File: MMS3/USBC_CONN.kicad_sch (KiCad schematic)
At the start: 7 parts, among them J800 USB_C_Receptacle_USB2.0_16P, U401 TPD2EUSB30DRTR-TP

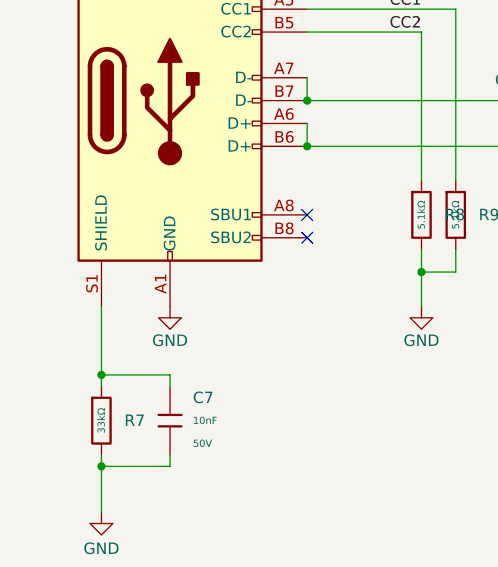
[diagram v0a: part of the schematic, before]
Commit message: schematic + partly layout
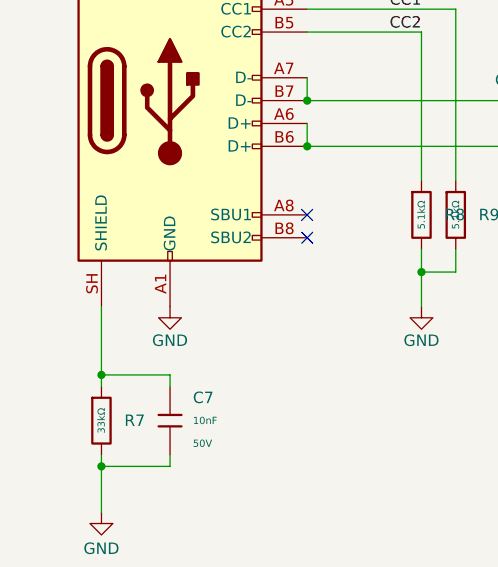
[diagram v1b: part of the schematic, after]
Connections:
- net at C7.1, R7.1: now also J800.SH (SHIELD); no longer J800.S1 (SHIELD)
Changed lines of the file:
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@@
 		(pin "B1"
 		)
-		(pin "S1"
+		(pin "SH"
 		)
 		(pin "A1"
